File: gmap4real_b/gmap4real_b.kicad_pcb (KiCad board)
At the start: 2 copper layers, 201.9 x 58.4 mm, 29 parts

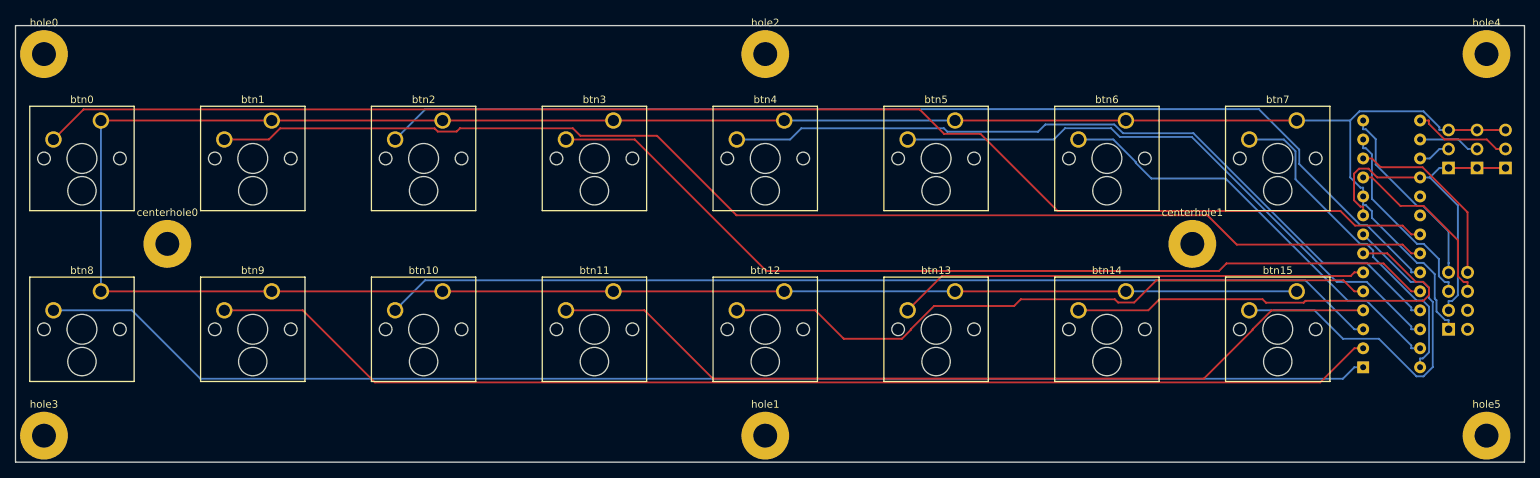
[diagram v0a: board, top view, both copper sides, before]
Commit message: smaller PCBs
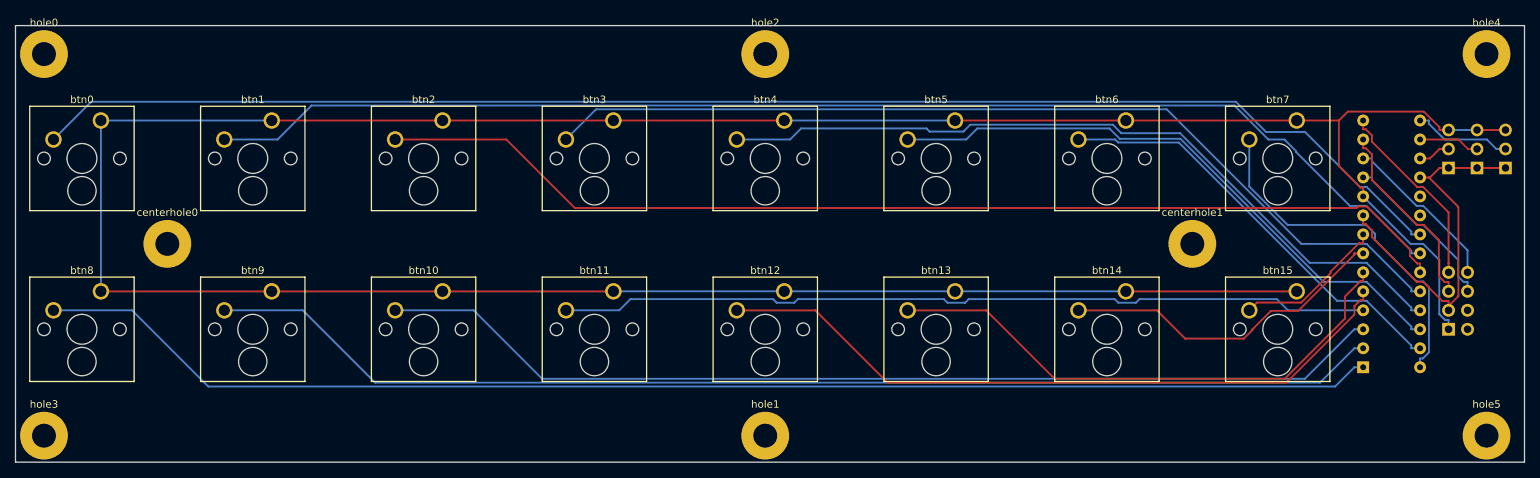
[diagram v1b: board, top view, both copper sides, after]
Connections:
- mcp23s17_0 pad 19: (no net) -> Net-(mcp23s17_0-Pad19)
- mcp23s17_0 pad 20: (no net) -> Net-(mcp23s17_0-Pad20)
- port0 pad 2: (no net) -> agnd
- port0 pad 4: (no net) -> Net-(port0-Pad4)
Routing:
- net btn15: track 51.3 -> 20.3 mm
- net btn14: track 59.8 -> 44.6 mm
- net btn13: track 63.1 -> 73.1 mm
- net btn11: track 114.3 -> 109.1 mm
- net btn12: track 89.6 -> 94.2 mm
- net btn02: track 149.2 -> 145.9 mm
- net btn07: track 44.9 -> 47.8 mm
- net sck: track 25.0 -> 22.2 mm
- net btn03: track 123.5 -> 126.3 mm
- net btn01: track 167.9 -> 170.4 mm
- net btn10: track 133.9 -> 136.1 mm
- net 3.3v: track 48.0 -> 49.9 mm
- net cs23s17: track 23.8 -> 22.5 mm
- net btn00: track 191.5 -> 192.5 mm
- net btn08: track 179.7 -> 180.6 mm
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
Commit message: button: even smaller
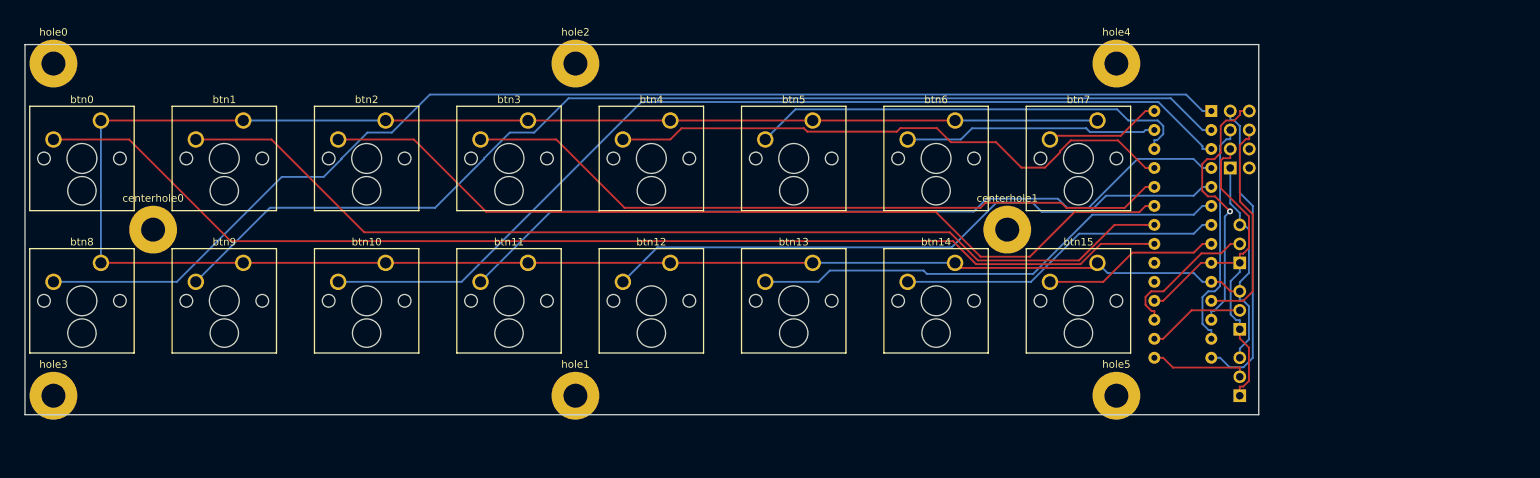
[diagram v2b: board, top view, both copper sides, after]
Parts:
- moved hole5 49.8 mm to (195.6, 104.1)
- moved hole4 49.5 mm to (195.6, 59.7)
- moved jmp_2 46.8 mm to (212.1, 104.1)
- moved mcp23s17_0 39.9 mm to (208.3, 66.0), turned to 180 degrees
- moved jmp_1 38.4 mm to (212.1, 95.2)
- moved port0 36.3 mm to (210.8, 73.7)
- moved jmp_0 30.7 mm to (212.1, 86.4)
- moved btn15 26.9 mm to (193.0, 86.4)
- moved btn7 26.7 mm to (193.0, 67.3)
- moved hole1 26.0 mm to (123.2, 104.1)
- moved hole2 25.4 mm to (123.2, 59.7)
- moved centerhole1 24.8 mm to (181.0, 81.9)
- moved btn14 23.2 mm to (174.0, 86.4)
- moved btn6 22.9 mm to (174.0, 67.3)
- moved btn13 19.4 mm to (154.9, 86.4)
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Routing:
- net gnd: track 408.1 -> 335.8 mm
- net btn00: track 192.5 -> 155.4 mm
- net btn01: track 170.4 -> 136.9 mm
- net btn07: track 47.8 -> 15.5 mm
- net btn03: track 126.3 -> 95.7 mm
- net btn02: track 145.9 -> 118.5 mm
- net btn04: track 103.1 -> 77.4 mm
- net btn06: track 57.5 -> 34.0 mm
- net btn05: track 80.5 -> 59.7 mm
- net miso: track 25.7 -> 41.2 mm
- net Net-(jmp_0-Pad2): track 4.34 -> 19.3 mm
- net btn08: track 180.6 -> 166.3 mm
- net sck: track 22.2 -> 35.9 mm, vias 0 -> 1
- net btn09: track 158.3 -> 147.9 mm
- net btn12: track 94.2 -> 85.0 mm
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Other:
- board size 201.9 x 58.4 mm -> 165.1 x 49.5 mm
